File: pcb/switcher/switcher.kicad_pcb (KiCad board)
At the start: 2 copper layers, 37.4 x 47.4 mm, 36 parts, among them J4 Conn_01x02, J5 OUT, J6 Input, J8 I2C, J9 I2C, SW7 reset, SW8 set, SW9 toggle, U2 SLG47115V

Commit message: Preparing switcher for fabrication.
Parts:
- renumbered C20 to C1, C19 to C2, C22 to C3, C14 to C4, C16 to C5, C18 to C6, D4 to D1, D3 to D2, D2 to D3, D6 to D4, J6 to J1, J5 to J2, J4 to J3, J8 to J4, J9 to J5, NT4 to NT1, NT5 to NT2, NT2 to NT3, NT3 to NT4, R4 to R1, R3 to R2, R2 to R3, R6 to R4, R7 to R6, R8 to R7, SW9 to SW1, SW7 to SW2, SW8 to SW3, U2 to U1
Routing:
- net 3V3: track 91.4 -> 89.7 mm
- net HV-GND: vias 2 -> 3
- net GND: vias 5 -> 6
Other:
- board text added: "12-24V"
- board text removed: "PWR IN 12-24V"

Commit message: Adding issues after live testing and soldering.
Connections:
- U1 pad 12: unconnected-(U1-SENSE2-Pad12) -> HV-GND
- U1 pad 5: unconnected-(U1-SENSE1-Pad5) -> HV-GND
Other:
- board text added: "Wires-first switcher v${VERSION} Copyright (c) devbotas"
- board text removed: "Wires-first switcher v0.4.0 Copyright (c) devbotas"

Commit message: Playing with text tags.
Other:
- board text added: "${TITLE} v${VERSION} Copyright (c) ${COMPANY}"
- board text removed: "Wires-first switcher v${VERSION} Copyright (c) devbotas"
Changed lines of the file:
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@@
 	(paper "A4")
 	(title_block
+		(title "${TITLE}")
 		(rev "${VERSION}")
+		(company "${COMPANY}")
 	)
 	(layers
@@
 		)
 	)
+	(property "COMPANY" "devbotas")
+	(property "TITLE" "Wires-first Switcher")
 	(property "VERSION" "0.4.1")
 	(footprint "Capacitor_SMD:C_0603_1608Metric"
@@
 		)
 	)
-	(gr_text "Wires-first\nswitcher v${VERSION}\nCopyright \n(c) devbotas\n"
+	(gr_text "${TITLE}\nv${VERSION}\nCopyright \n(c) ${COMPANY}\n"
 		(at 82.5 132 0)
 		(layer "F.SilkS")

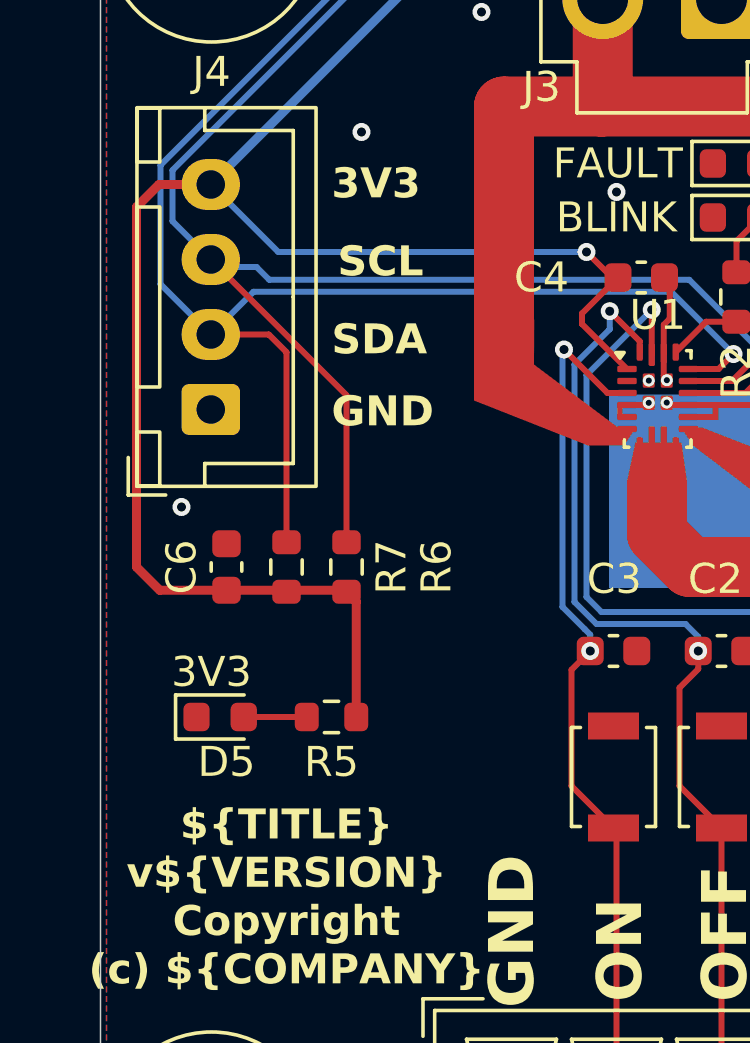
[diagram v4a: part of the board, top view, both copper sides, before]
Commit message: Adding solderable jumbers for I2C pullups in Switcher.
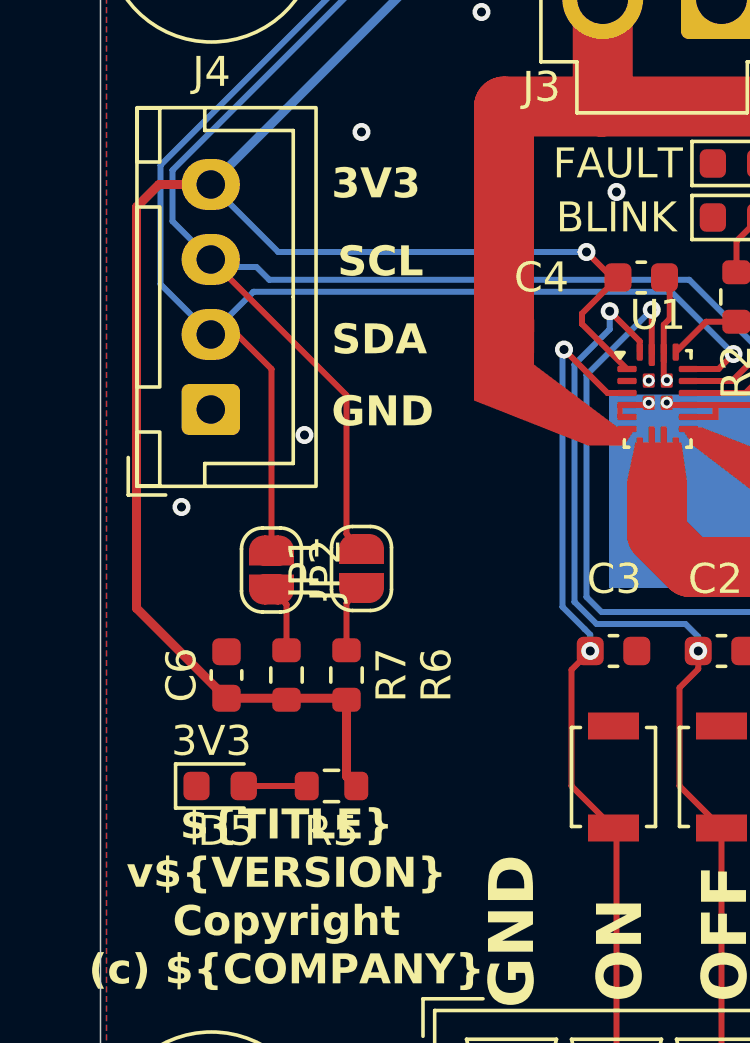
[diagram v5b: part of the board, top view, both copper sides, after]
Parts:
- added JP1: SolderJumper_2_Open, Jumper:SolderJumper-2_P1.3mm_Open_RoundedPad1.0x1.5mm, F.Cu at (85.0, 121.0)
- added JP2: SolderJumper_2_Open, Jumper:SolderJumper-2_P1.3mm_Open_RoundedPad1.0x1.5mm, F.Cu at (82.0, 121.1)
- moved C6 3.60 mm to (80.5, 124.6)
- moved R6 3.60 mm to (84.5, 124.6)
- moved R7 3.60 mm to (82.5, 124.6)
- moved D5 2.30 mm to (80.3, 128.3)
- moved R5 2.30 mm to (84.0, 128.3)
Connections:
- R6 pad 2: SCL -> Net-(JP1-B)
- R7 pad 2: SDA -> Net-(JP2-B)
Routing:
- net Net-(JP1-B): track 0.00 -> 2.28 mm
- net Net-(JP2-B): track 0.00 -> 2.23 mm
- net 3V3: track 89.7 -> 90.7 mm
- net SDA: track 78.4 -> 77.8 mm
- net GND: vias 6 -> 7

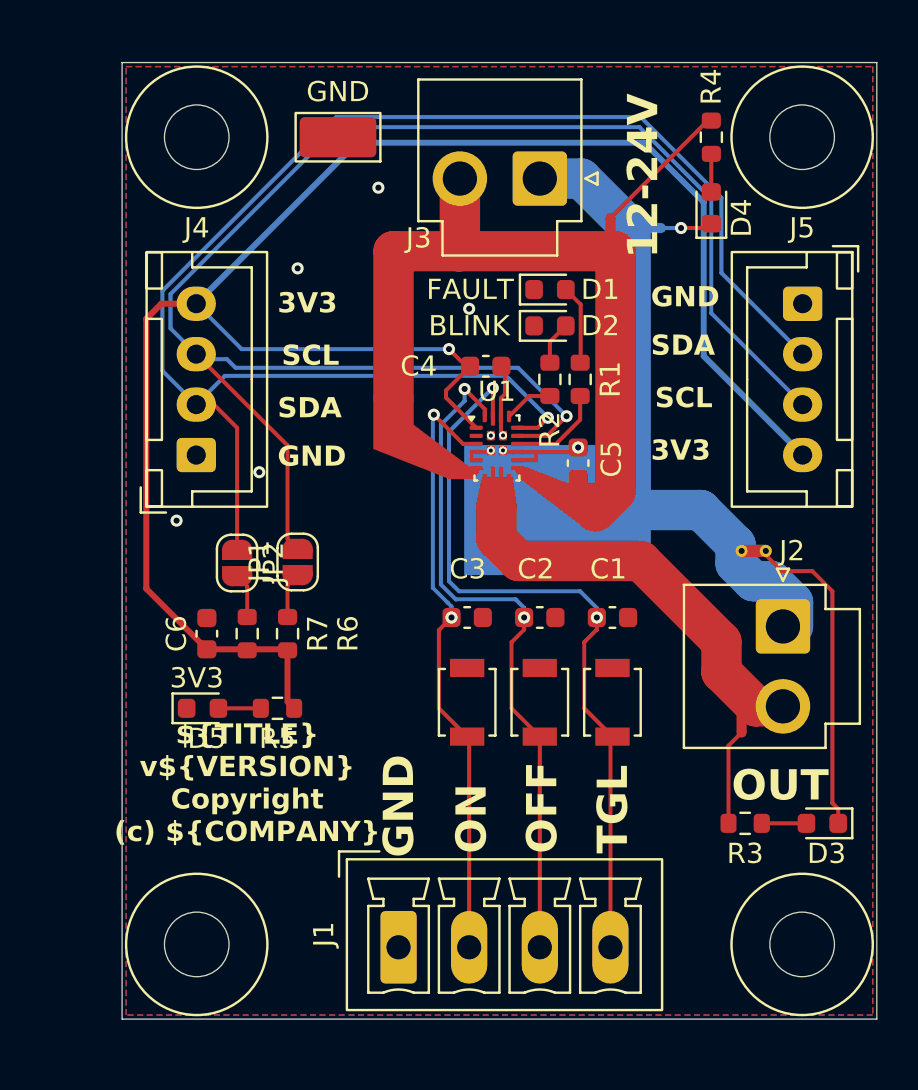
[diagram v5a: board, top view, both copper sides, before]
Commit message: Switcher: adding protection resistors.
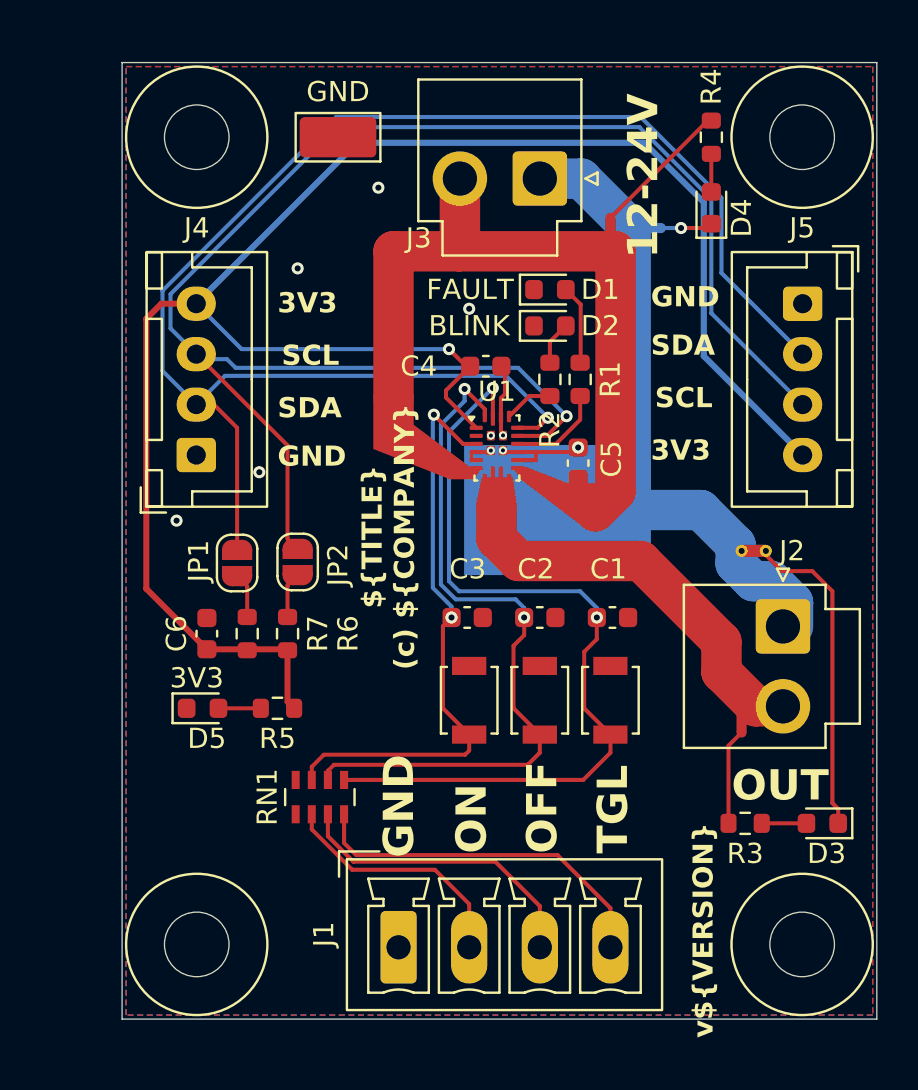
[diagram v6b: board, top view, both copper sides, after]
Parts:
- added RN1: R_Pack04, Resistor_SMD:R_Array_Concave_4x0603, F.Cu at (86.1, 132.7)
- moved SW1 0.14 mm to (100.5, 127.9)
- moved SW3 0.14 mm to (93.5, 127.9)
- moved SW2 0.10 mm to (97.0, 127.9)
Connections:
- C1 pad 2: Net-(J1-Pin_4) -> Net-(RN1-R4.2)
- C2 pad 2: Net-(J1-Pin_3) -> Net-(RN1-R3.2)
- C3 pad 2: Net-(J1-Pin_2) -> Net-(RN1-R2.2)
- SW1 pad 2: Net-(J1-Pin_4) -> Net-(RN1-R4.2)
- SW2 pad 2: Net-(J1-Pin_3) -> Net-(RN1-R3.2)
- SW3 pad 2: Net-(J1-Pin_2) -> Net-(RN1-R2.2)
- U1 pad 19: Net-(J1-Pin_4) -> Net-(RN1-R4.2)
- U1 pad 20: Net-(J1-Pin_3) -> Net-(RN1-R3.2)
- U1 pad 3: Net-(J1-Pin_2) -> Net-(RN1-R2.2)
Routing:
- net Net-(RN1-R4.2): track 0.00 -> 41.6 mm, vias 0 -> 2
- net Net-(RN1-R3.2): track 0.00 -> 35.8 mm, vias 0 -> 2
- net Net-(RN1-R2.2): track 0.00 -> 29.4 mm, vias 0 -> 2
- net Net-(J1-Pin_4): track 37.9 -> 17.9 mm, vias 2 -> 0
- net Net-(J1-Pin_3): track 34.4 -> 15.1 mm, vias 2 -> 0
- net Net-(J1-Pin_2): track 30.4 -> 12.2 mm, vias 2 -> 0
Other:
- board text added: "${TITLE}"
- board text added: "(c) ${COMPANY}"
- board text added: "v${VERSION}"
- board text removed: "${TITLE} v${VERSION} Copyright (c) ${COMPANY}"

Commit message: Switcher: fixing ERC/DRC issues.
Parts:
- moved C6 0.40 mm to (80.1, 124.6)
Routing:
- net 3V3: track 90.7 -> 91.6 mm
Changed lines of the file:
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@@
 	(footprint "Capacitor_SMD:C_0603_1608Metric"
 		(layer "F.Cu")
-		(at 80.5 124.6 90)
+		(at 80.1 124.6 90)
 		(descr "Capacitor SMD 0603 (1608 Metric), square (rectangular) end terminal, IPC-7351 nominal, (Body size source: IPC-SM-782 page 76, https://www.pcb-3d.com/wordpress/wp-content/uploads/ipc-sm-782a_amendment_1_and_2.pdf)")
 		(tags "capacitor")
@@
 	)
 	(segment
-		(start 84.5 127.975)
-		(end 84.825 128.3)
+		(start 78.25 108.25)
+		(end 77.5 109)
 		(width 0.3)
 		(layer "F.Cu")
@@
 	)
 	(segment
-		(start 93.35 111.35)
-		(end 92.5 110.5)
-		(width 0.2)
+		(start 78.975 125.375)
+		(end 80.5 125.375)
+		(width 0.3)
 		(layer "F.Cu")
 		(net "3V3")
 	)
 	(segment
-		(start 77.5 122.375)
-		(end 80.5 125.375)
+		(start 84.5 127.975)
+		(end 84.825 128.3)
 		(width 0.3)
 		(layer "F.Cu")
@@
 	)
 	(segment
+		(start 93.35 111.35)
+		(end 92.5 110.5)
+		(width 0.2)
+		(layer "F.Cu")
+		(net "3V3")
+	)
+	(segment
 		(start 79.975 108.25)
 		(end 78.25 108.25)
@@
 	)
 	(segment
-		(start 78.25 108.25)
-		(end 77.5 109)
+		(start 77.5 109)
+		(end 77.5 123.9)
 		(width 0.3)
 		(layer "F.Cu")
@@
 	)
 	(segment
-		(start 77.5 109)
-		(end 77.5 122.375)
+		(start 77.5 123.9)
+		(end 78.975 125.375)
 		(width 0.3)
 		(layer "F.Cu")

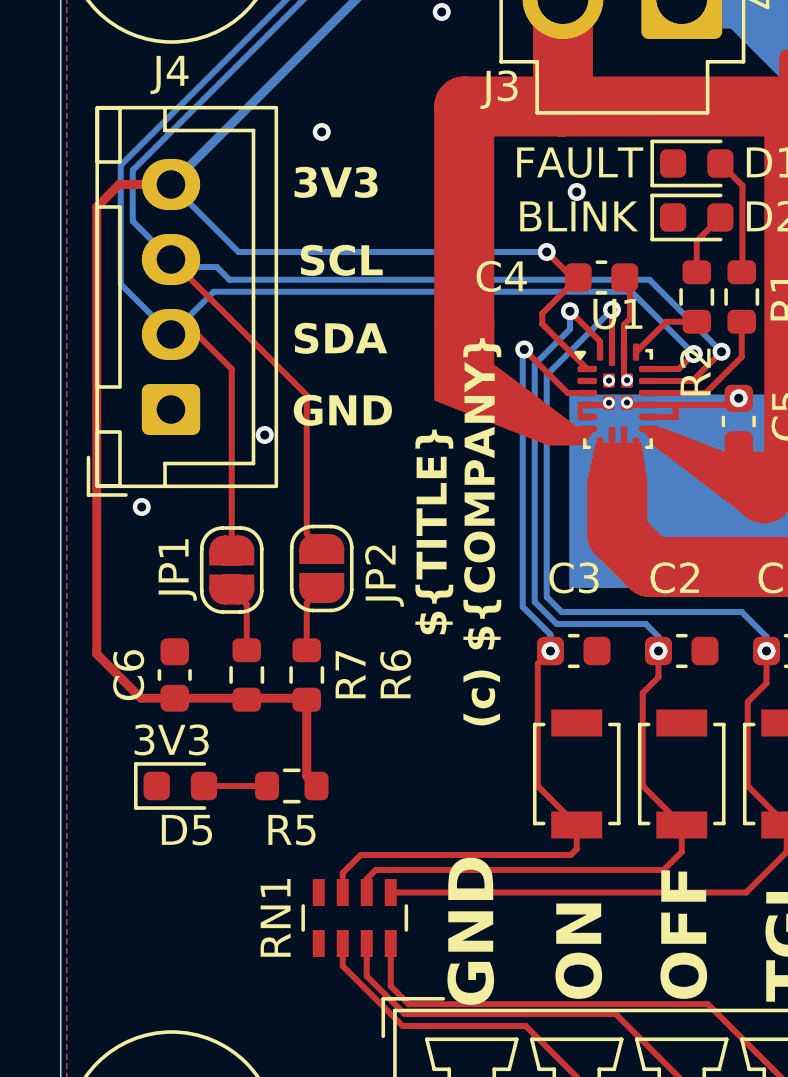
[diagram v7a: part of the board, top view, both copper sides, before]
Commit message: Switcher: Using PIN3 on SLG to select I2C bit3.
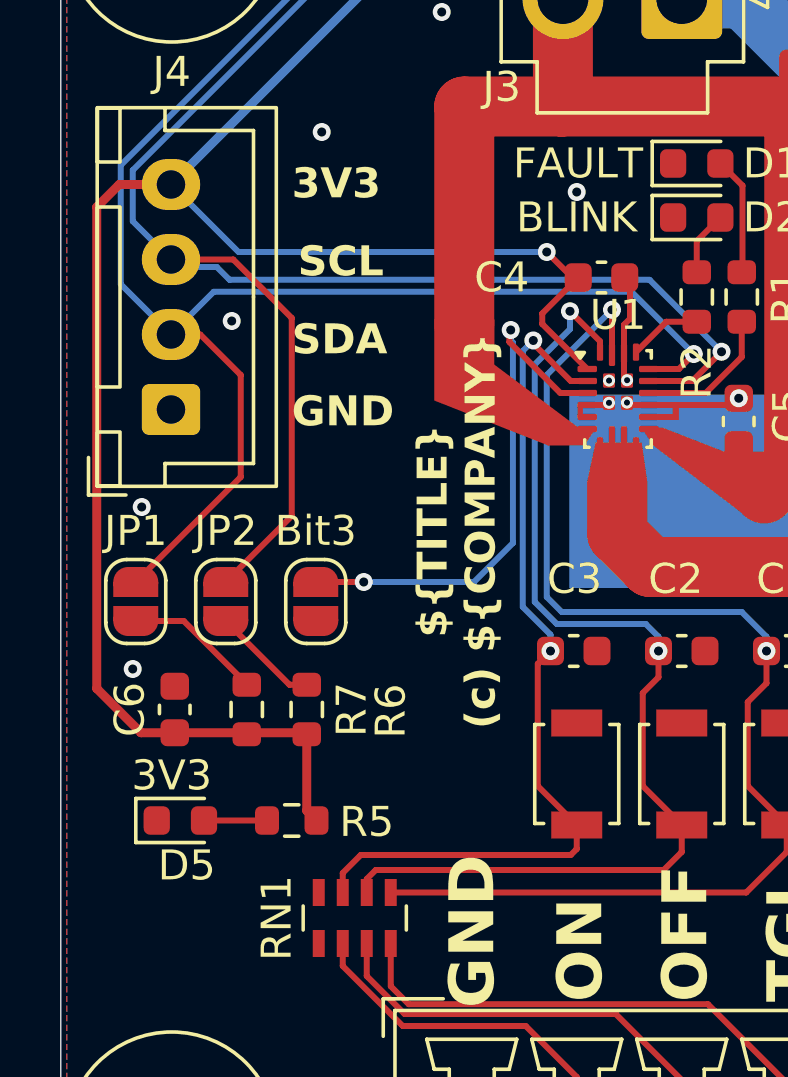
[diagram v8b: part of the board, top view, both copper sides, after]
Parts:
- added Bit3: SolderJumper_2_Open, Jumper:SolderJumper-2_P1.3mm_Open_RoundedPad1.0x1.5mm, F.Cu at (84.8, 122.2)
- moved JP1 3.38 mm to (81.8, 122.2)
- moved JP2 3.37 mm to (78.8, 122.2)
- moved C6 1.15 mm to (80.1, 125.8)
- moved R6 1.15 mm to (84.5, 125.8)
- moved R7 1.15 mm to (82.5, 125.8)
- moved D5 1.15 mm to (80.3, 129.4)
- moved R5 1.15 mm to (84.0, 129.4)
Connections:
- U1 pad 2: unconnected-(U1-GPIO0-Pad2) -> Net-(RN1-R2.2)
- U1 pad 3: Net-(RN1-R2.2) -> Net-(Bit3-B)
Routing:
- net Net-(Bit3-B): track 0.00 -> 18.0 mm, vias 0 -> 2
- net SCL: track 81.5 -> 84.3 mm
- net SDA: track 77.8 -> 80.5 mm
- net Net-(JP2-B): track 2.23 -> 4.59 mm
- net Net-(JP1-B): track 2.28 -> 3.58 mm
- net 3V3: track 91.6 -> 92.7 mm
- net GND: vias 7 -> 8
